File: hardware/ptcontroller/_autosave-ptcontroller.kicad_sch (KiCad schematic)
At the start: 2 parts

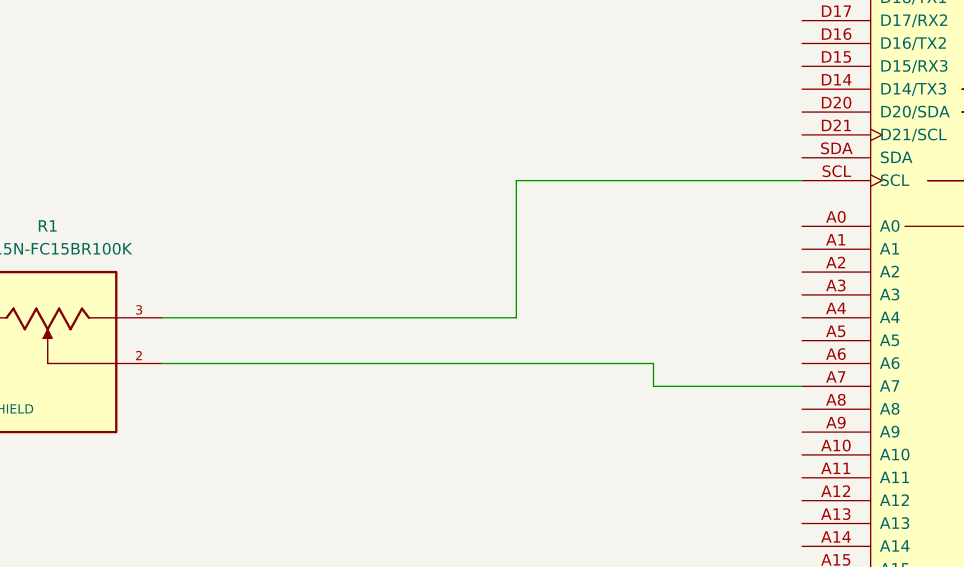
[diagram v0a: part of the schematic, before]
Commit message: added pot
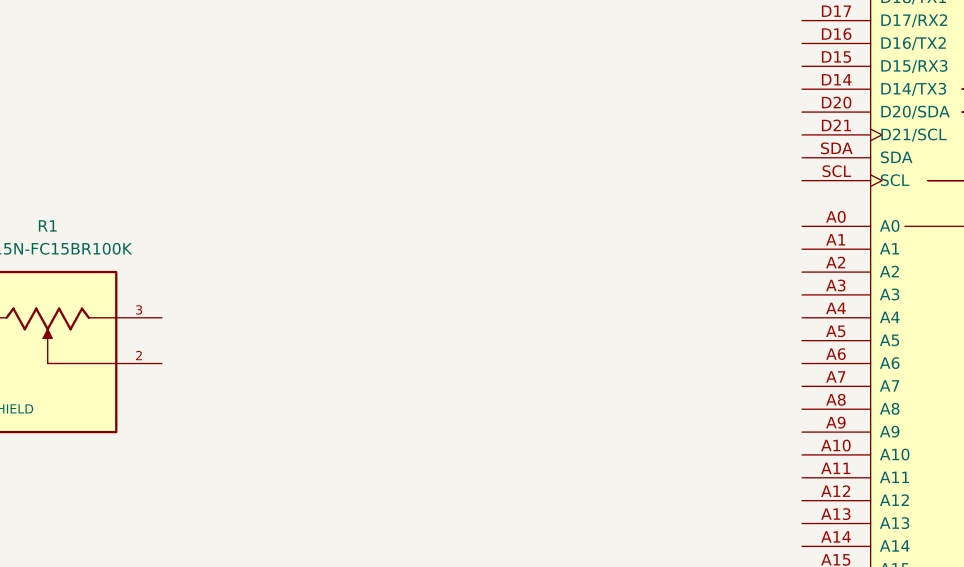
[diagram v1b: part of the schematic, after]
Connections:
- net at R1.2: no longer A1.A7
- net at R1.3: no longer A1.SCL
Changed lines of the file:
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@@
 (kicad_sch (version 20230121) (generator eeschema)
   (paper "A4")
-  (wire (pts (xy 118.11 85.09) (xy 172.72 85.09))
-    (stroke (width 0) (type default))
-  )
-  (wire (pts (xy 172.72 87.63) (xy 189.23 87.63))
-    (stroke (width 0) (type default))
-  )
-  (wire (pts (xy 157.48 80.01) (xy 157.48 64.77))
-    (stroke (width 0) (type default))
-  )
-  (wire (pts (xy 157.48 64.77) (xy 189.23 64.77))
-    (stroke (width 0) (type default))
-  )
-  (wire (pts (xy 118.11 80.01) (xy 157.48 80.01))
-    (stroke (width 0) (type default))
-  )
-  (wire (pts (xy 172.72 85.09) (xy 172.72 87.63))
-    (stroke (width 0) (type default))
-  )
   (symbol (lib_id "P0915N-FC15BR100K:P0915N-FC15BR100K") (at 105.41 82.55 0) (unit 1)
     (in_bom yes) (on_board yes) (dnp no) (fields_autoplaced)
